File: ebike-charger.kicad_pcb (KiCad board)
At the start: 2 copper layers, 2 parts, among them U1 CH224K, U3 LM5050-1

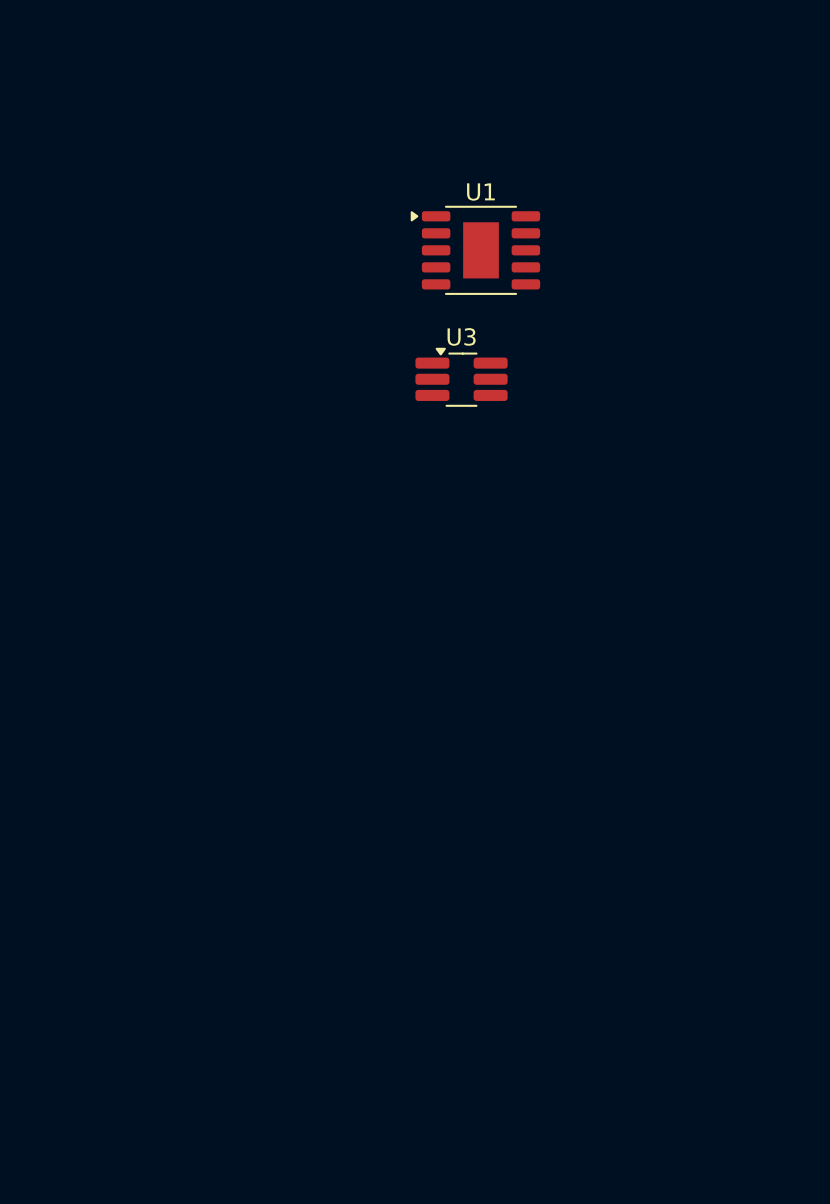
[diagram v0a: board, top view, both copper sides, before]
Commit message: added ideal diode
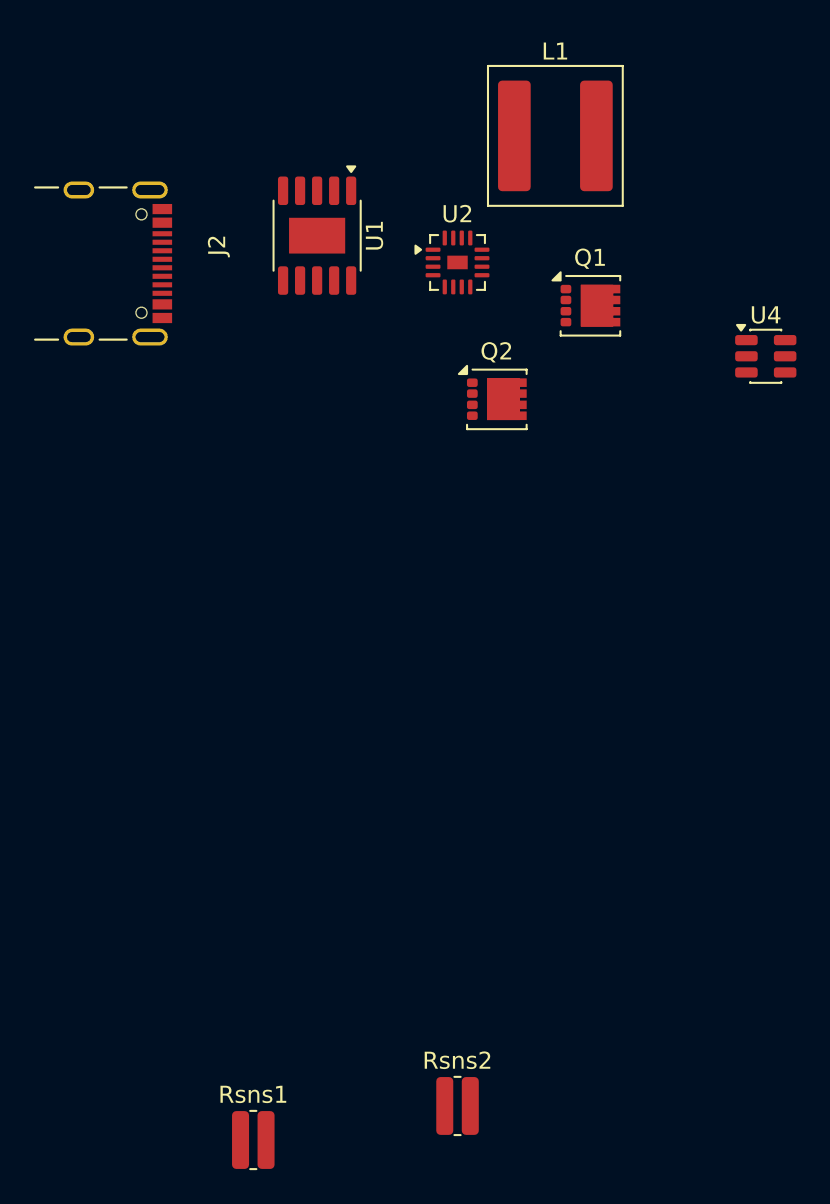
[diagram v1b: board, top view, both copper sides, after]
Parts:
- removed U3: LM5050-1, Package_TO_SOT_SMD:TSOT-23-6_HandSoldering
- added J2: UJ20-C-H-G-SMT-2A-P16-TR, SnapEDA:SAMESKY_UJ20-C-H-G-SMT-2A-P16-TR, F.Cu at (41.5, 71.0)
- added L1: 8.2uH/14.5mR, Inductor_SMD:L_Coilcraft_XAL7070-XXX, F.Cu at (69.5, 63.5)
- added Q1: CSD18543Q3A, Package_SON:VSON-8_3.3x3.3mm_P0.65mm_NexFET, F.Cu at (71.6, 73.5)
- added Q2: CSD18543Q3A, Package_SON:VSON-8_3.3x3.3mm_P0.65mm_NexFET, F.Cu at (66.1, 79.0)
- added Rsns1: 8mR, Resistor_SMD:R_0612_1632Metric, F.Cu at (51.8, 122.5)
- added Rsns2: 8mR, Resistor_SMD:R_0612_1632Metric, F.Cu at (63.8, 120.5)
- added U2: TPS43060RTER, Package_DFN_QFN:Texas_RTE_WQFN-16-1EP_3x3mm_P0.5mm_EP1.2x0.8mm, F.Cu at (63.8, 70.9)
- added U4: LM74700, Package_TO_SOT_SMD:SOT-23-6, F.Cu at (81.9, 76.5)
- moved U1 9.67 mm to (55.5, 69.4), turned to -90 degrees
